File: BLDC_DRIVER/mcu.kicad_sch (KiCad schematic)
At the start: 45 parts, among them J101 Conn_01x05_Pin, J102 Conn_01x03_Pin, J103 Conn_01x03_Pin, SW1 SW_Push_Dual_x2, SW2 SW_Push_Dual_x2, SW3 SW_Push_Dual_x2, SW4 SW_Push_Dual_x2, SW5 SW_Push_Dual_x2, U101 ESP32-S3-WROOM-1U-N16R2, U2 STM32G431RBTx, Y1 Crystal

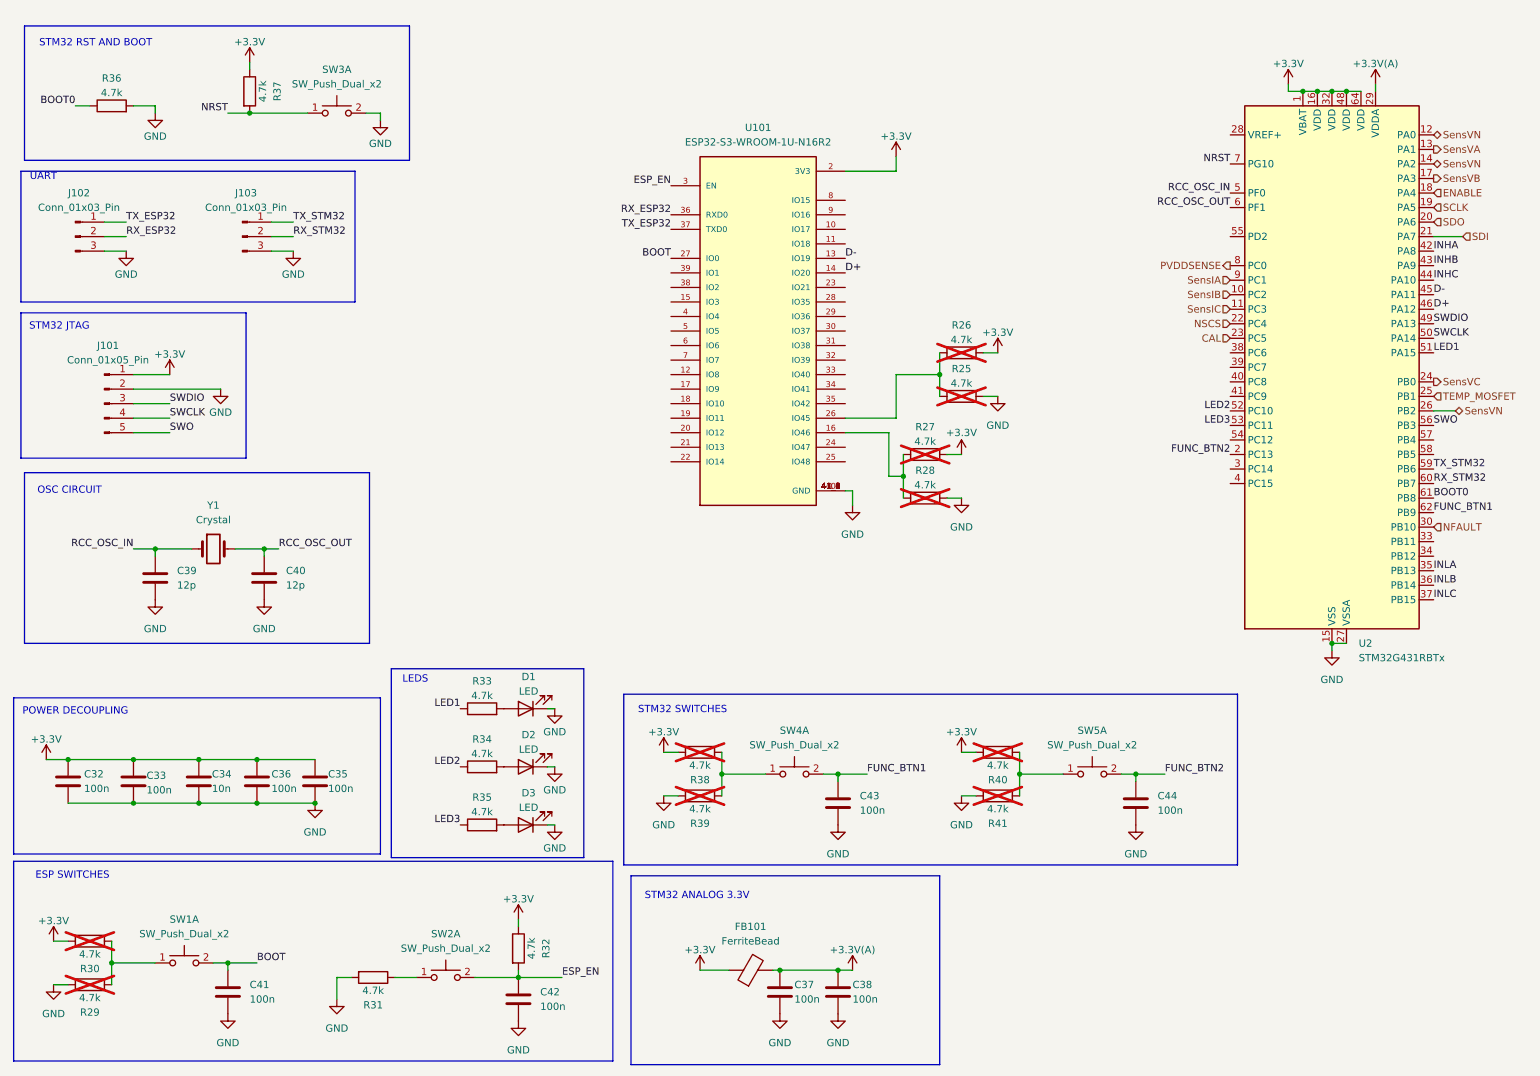
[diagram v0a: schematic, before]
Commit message: footprints added, cap values corrected
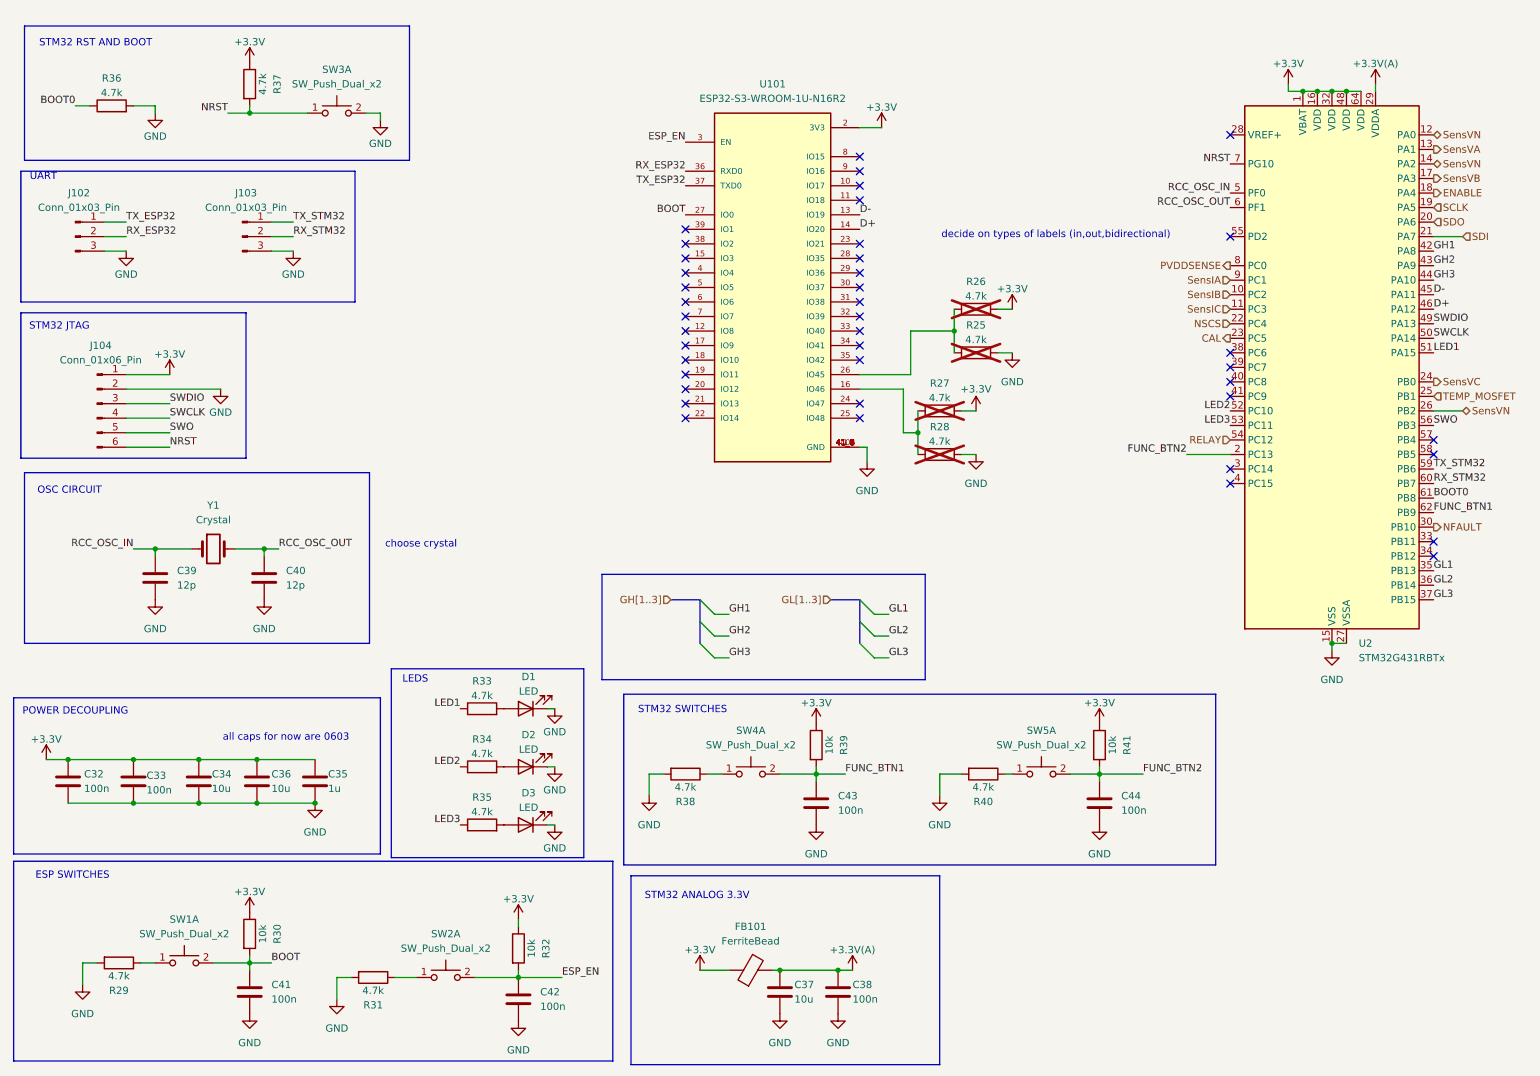
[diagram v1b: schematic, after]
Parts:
- removed J101: Conn_01x05_Pin, symbol Connector:Conn_01x05_Pin
- added J104: Conn_01x06_Pin, Connector_PinHeader_2.54mm:PinHeader_1x06_P2.54mm_Vertical, symbol Connector:Conn_01x06_Pin
- C32, C33, C38, C39, C40, C41, C42, C43, C44: footprint (none) -> Capacitor_SMD:C_0603_1608Metric_Pad1.08x0.95mm_HandSolder
- C34: value 10n -> 10u; footprint (none) -> Capacitor_SMD:C_0603_1608Metric_Pad1.08x0.95mm_HandSolder
- C35: value 100n -> 1u; footprint (none) -> Capacitor_SMD:C_0603_1608Metric_Pad1.08x0.95mm_HandSolder
- C36, C37: value 100n -> 10u; footprint (none) -> Capacitor_SMD:C_0603_1608Metric_Pad1.08x0.95mm_HandSolder
- D1, D2, D3: footprint (none) -> Diode_SMD:D_SOD-123
- FB101: footprint (none) -> Inductor_SMD:L_0805_2012Metric_Pad1.05x1.20mm_HandSolder
- J102, J103: footprint (none) -> Connector_PinHeader_2.54mm:PinHeader_1x03_P2.54mm_Vertical
- R29, R38, R40: footprint (none) -> Resistor_SMD:R_0603_1608Metric_Pad0.98x0.95mm_HandSolder; now fitted
- R30, R39, R41: value 4.7k -> 10k; footprint (none) -> Resistor_SMD:R_0603_1608Metric_Pad0.98x0.95mm_HandSolder; now fitted
- R31, R33, R34, R35, R36, R37: footprint (none) -> Resistor_SMD:R_0603_1608Metric_Pad0.98x0.95mm_HandSolder
- R32: value 4.7k -> 10k; footprint (none) -> Resistor_SMD:R_0603_1608Metric_Pad0.98x0.95mm_HandSolder
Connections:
- net +3.3V: now also R30.1, R39.1, R41.1, J104.1 (Pin_1); no longer R30.2, R38.2, R40.2
- net BOOT: now also R30.2
- net FUNC_BTN1: now also R39.2
- net FUNC_BTN2: now also R41.2
- net GND: now also R38.2, R40.2, J104.2 (Pin_2); no longer R39.2, R41.2
- net NRST: now also J104.6 (Pin_6)
- net SWCLK: now also J104.4 (Pin_4)
- net SWDIO: now also J104.3 (Pin_3)
- net SWO: now also J104.5 (Pin_5)
- net at R29.1, SW1.1 (C): no longer R30.1
- net RELAY: now reaches U2.54 (PC12)
- net at R38.1, SW4.1 (C): no longer R39.1
- net at R40.1, SW5.1 (C): no longer R41.1
- net INHA renamed GH1
- net INHB renamed GH2
- net INHC renamed GH3
- net INLA renamed GL1
- net INLB renamed GL2
- net INLC renamed GL3
- no-connect marks 0 -> 41
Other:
- note added: "all caps for now are 0603"
- note added: "choose crystal"
- note added: "decide on types of labels (in,out,bidirectional)"
- moved on the sheet: C41, C43, C44, R25, R26, R27, R28, R37, SW4A, SW5A, U101

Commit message: buck changed and calculated
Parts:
- renumbered C33 to C10, C39 to C11, C34 to C12, C41 to C13, C36 to C14, C40 to C15, C35 to C16, C42 to C17, C37 to C18, C38 to C19, C43 to C20, C44 to C21, C32 to C9, D1 to D2, D2 to D3, D3 to D4, FB101 to FB1, J102 to J2, J104 to J3, J103 to J4, R32 to R10, R33 to R11, R34 to R12, R35 to R13, R38 to R14, R39 to R15, R27 to R16, R28 to R17, R26 to R18, R25 to R19, R40 to R20, R41 to R21, R36 to R5, R37 to R6, R29 to R7, R30 to R8, R31 to R9, SW3 to SW2, SW2 to SW3, U101 to U2, U2 to U4

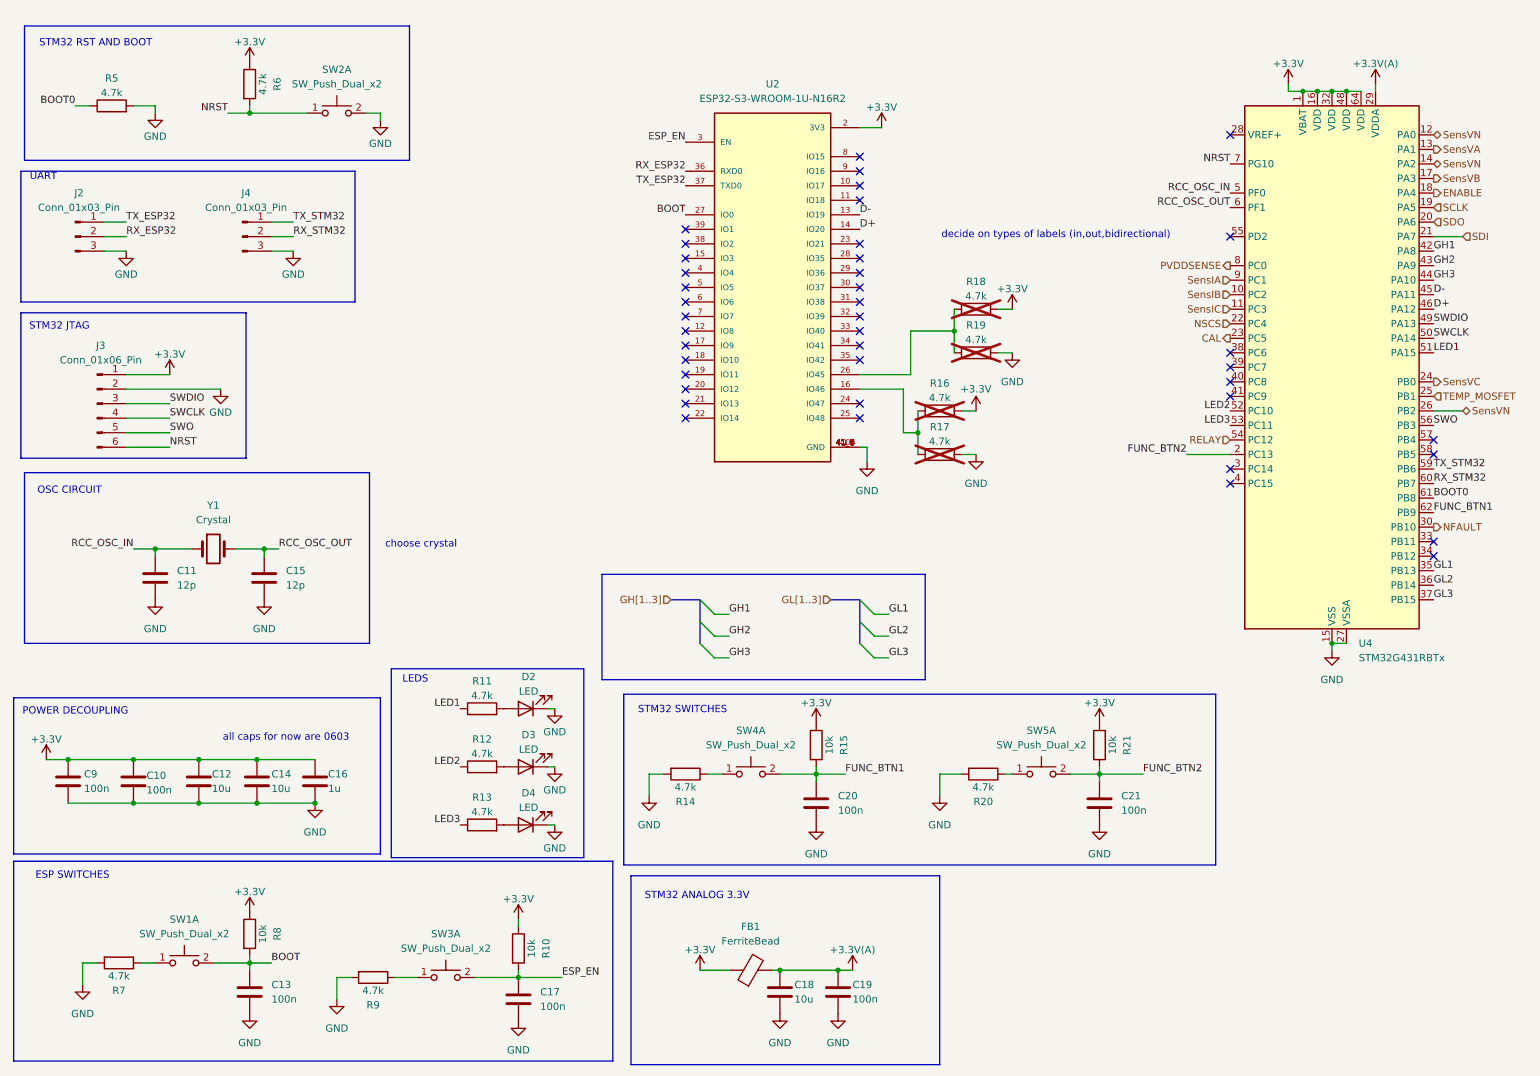
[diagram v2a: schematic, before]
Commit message: fuses and missing footprints added, labels cleaned
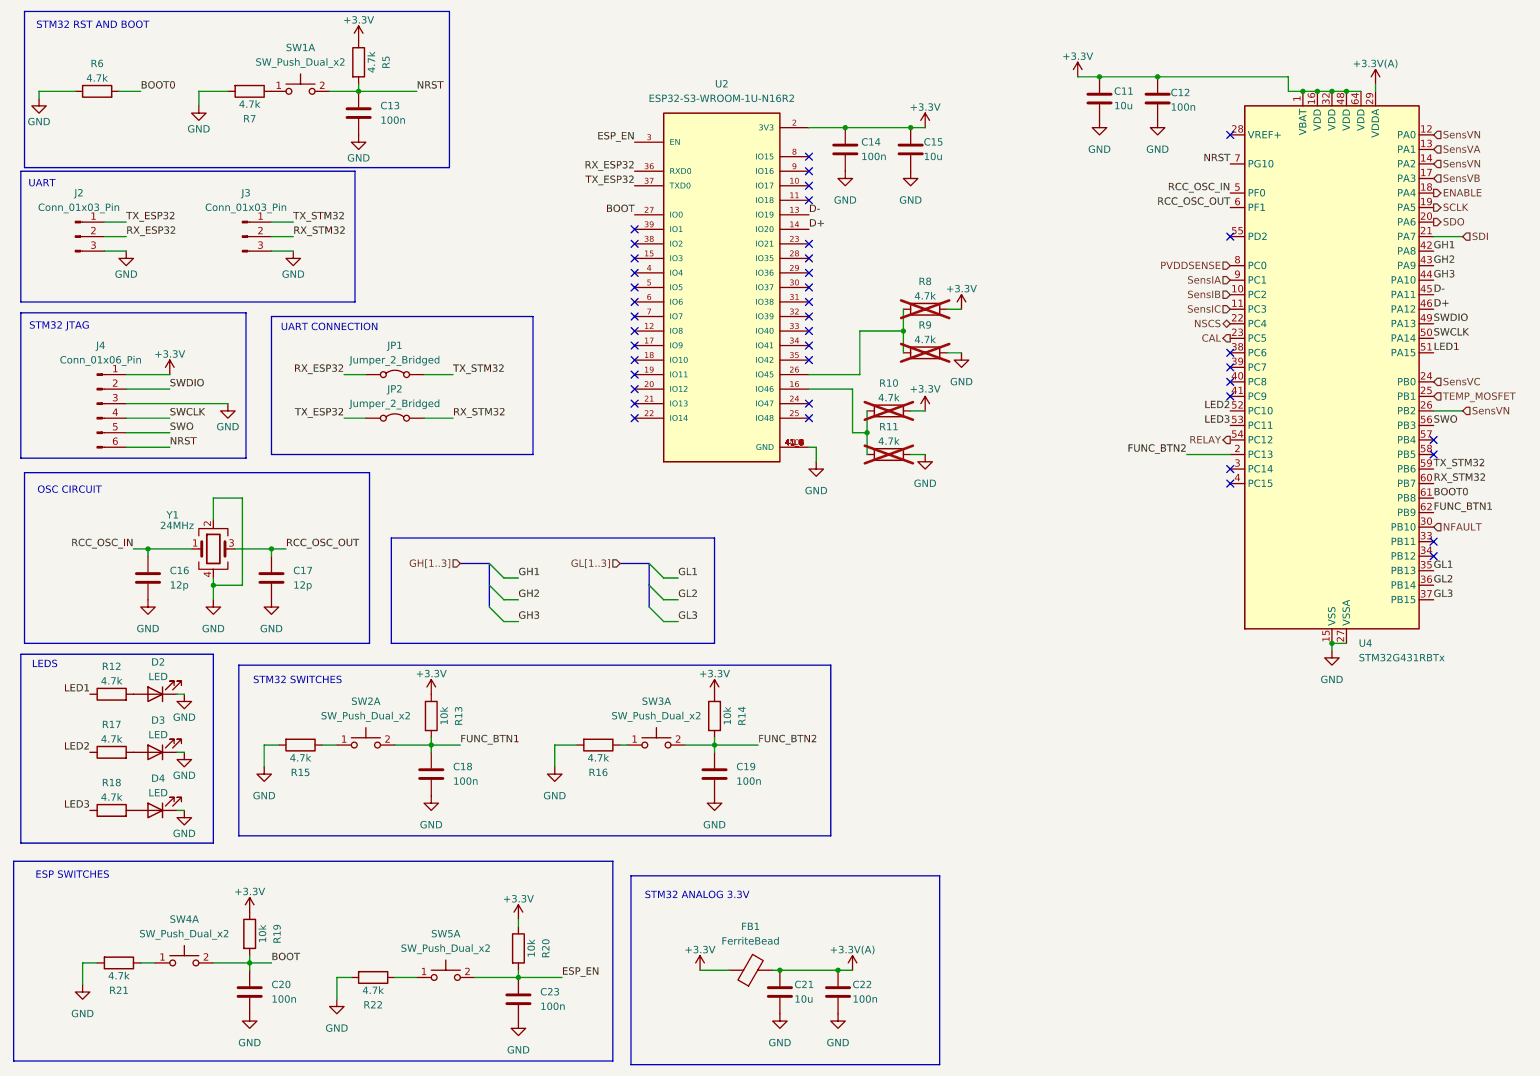
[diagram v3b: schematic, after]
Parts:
- removed C16: 1u, Capacitor_SMD:C_0603_1608Metric_Pad1.08x0.95mm_HandSolder, symbol Device:C
- removed Y1: Crystal, symbol Device:Crystal
- added C13: 100n, Capacitor_SMD:C_0603_1608Metric_Pad1.08x0.95mm_HandSolder, symbol Device:C
- added JP1, JP2: Jumper_2_Bridged, Jumper:SolderJumper-2_P1.3mm_Open_TrianglePad1.0x1.5mm, symbol Jumper:Jumper_2_Bridged
- added R7: 4.7k, Resistor_SMD:R_0603_1608Metric_Pad0.98x0.95mm_HandSolder, symbol Device:R
- added Y1: 24MHz, Crystal:Crystal_SMD_3225-4Pin_3.2x2.5mm, symbol Device:Crystal_GND24
- D2, D3, D4: footprint Diode_SMD:D_SOD-123 -> Diode_SMD:D_0805_2012Metric_Pad1.15x1.40mm_HandSolder
- renumbered C14 to C11, C10 to C12, C9 to C14, C12 to C15, C11 to C16, C15 to C17, C20 to C18, C21 to C19, C13 to C20, C18 to C21, C19 to C22, C17 to C23, J4 to J3, J3 to J4, R16 to R10, R17 to R11, R11 to R12, R15 to R13, R21 to R14, R14 to R15, R20 to R16, R12 to R17, R13 to R18, R8 to R19, R10 to R20, R7 to R21, R9 to R22, R6 to R5, R5 to R6, R18 to R8, R19 to R9, SW2 to SW1, SW4 to SW2, SW5 to SW3, SW1 to SW4, SW3 to SW5
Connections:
- net BOOT0: now also R6.2; no longer R6.1
- net GND: now also J4.3 (Pin_3), R6.1, C13.1, R7.2, Y1.2, Y1.4; no longer J4.2 (Pin_2), R6.2, SW1.2 (D)
- net NRST: now also SW1.2 (D), C13.2; no longer SW1.1 (C)
- net RCC_OSC_IN: now also Y1.1
- net RCC_OSC_OUT: now also Y1.3
- net RX_ESP32: now also JP1.1 (A)
- net RX_STM32: now also JP2.2 (B)
- net SWDIO: now also J4.2 (Pin_2); no longer J4.3 (Pin_3)
- net TX_ESP32: now also JP2.1 (A)
- net TX_STM32: now also JP1.2 (B)
- new net: R7.1, SW1.1 (C)
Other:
- note added: "UART CONNECTION"
- note removed: "POWER DECOUPLING"
- note removed: "all caps for now are 0603"
- note removed: "choose crystal"
- note removed: "decide on types of labels (in,out,bidirectional)"
- moved on the sheet: C11, C12, C14, C15, C16, C17, C18, C19, D2, D3, D4, R10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

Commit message: finall motor driver
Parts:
- R10, R11, R8, R9: footprint (none) -> Resistor_SMD:R_0603_1608Metric
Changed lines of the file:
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@@
 			)
 		)
-		(property "Footprint" ""
+		(property "Footprint" "Resistor_SMD:R_0603_1608Metric"
 			(at 172.72 74.168 90)
 			(effects
@@
 		(at 80.01 76.2 0)
 		(unit 1)
-		(exclude_from_sim yes)
+		(exclude_from_sim no)
 		(in_bom yes)
 		(on_board yes)
@@
 			)
 		)
-		(property "Footprint" ""
+		(property "Footprint" "Resistor_SMD:R_0603_1608Metric"
 			(at 166.37 84.328 90)
 			(effects
@@
 			)
 		)
-		(property "Footprint" ""
+		(property "Footprint" "Resistor_SMD:R_0603_1608Metric"
 			(at 172.72 66.548 90)
 			(effects
@@
 		(at 80.01 83.82 0)
 		(unit 1)
-		(exclude_from_sim yes)
+		(exclude_from_sim no)
 		(in_bom yes)
 		(on_board yes)
@@
 			)
 		)
-		(property "Footprint" ""
+		(property "Footprint" "Resistor_SMD:R_0603_1608Metric"
 			(at 166.37 91.948 90)
 			(effects
